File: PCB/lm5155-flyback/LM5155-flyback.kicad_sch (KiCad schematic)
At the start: 31 parts, among them Q1 DMT6030LFCL-7, T1 EP7-5801_750315825, U1 LM5155

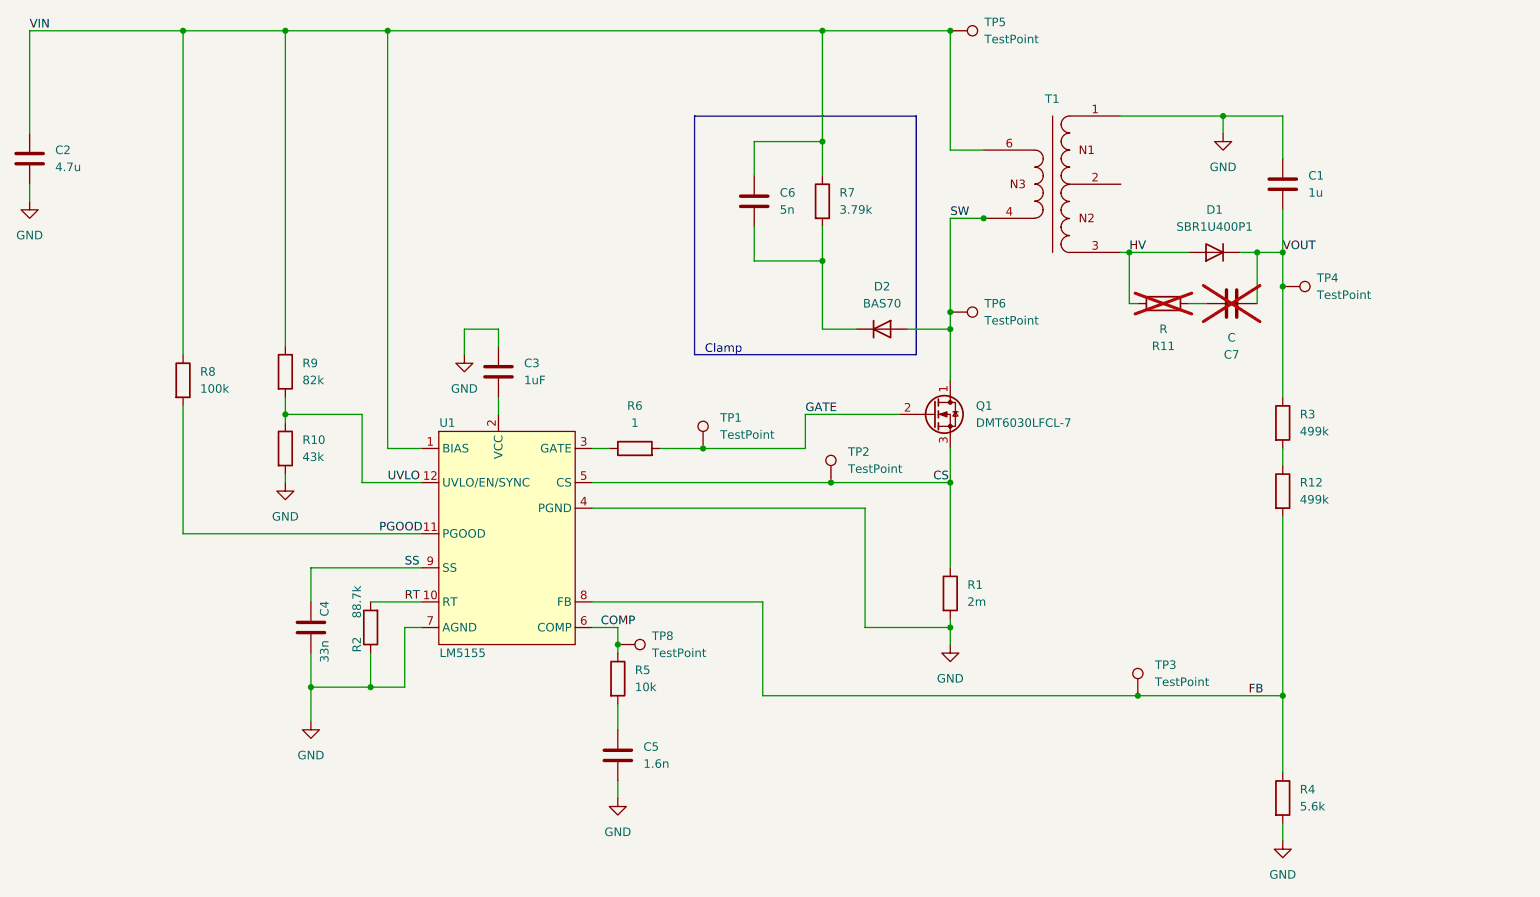
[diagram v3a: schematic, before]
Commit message: Replaced LM5155 with LM5156H. Also replaced MOSFET. Packages just too difficult to solder.
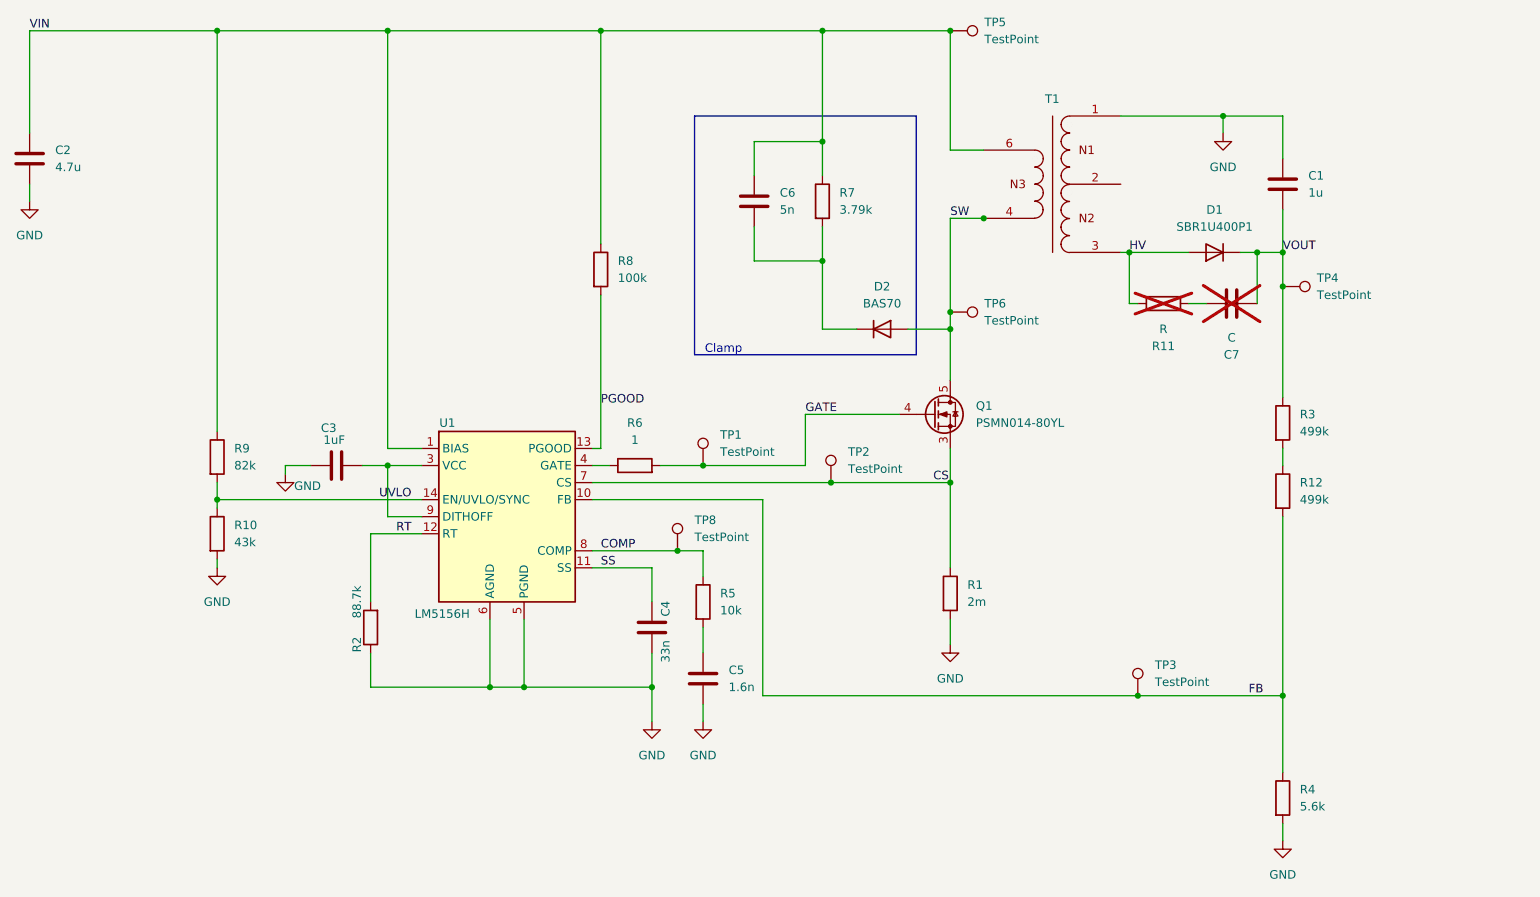
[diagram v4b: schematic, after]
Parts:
- removed Q1: DMT6030LFCL-7, LM5155-flyback:U-DFN1616-6, symbol Transistor_FET:Q_NMOS_DGS
- added Q1: PSMN014-80YL, Package_TO_SOT_SMD:LFPAK56, symbol LM5155-flyback:PSMN014-80YL
- U1: value LM5155 -> LM5156H; footprint LM5155-flyback:WSON-12-1EP_3x2mm_P0.5mm_EP1x2.65_ThermalVias -> Package_SO:Texas_HTSSOP-14-1EP_4.4x5mm_P0.65mm_EP3.4x5mm_Mask3.155x3.255mm_ThermalVias; symbol LM5155-flyback:LM5155 -> Regulator_Switching:LM5156HPWP
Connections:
- net COMP: now also U1.8 (COMP); no longer U1.6 (COMP)
- net CS: now also U1.7 (CS), Q1.1 (S), Q1.2 (S), Q1.3 (S); no longer U1.5 (CS)
- net FB: now also U1.10 (FB); no longer U1.8 (FB)
- net GATE: now also Q1.4 (G)
- net GND: now also U1.15 (AGND), U1.5 (PGND), U1.6 (AGND); no longer U1.13, U1.4 (PGND), U1.7 (AGND)
- net PGOOD: now also U1.13 (PGOOD); no longer U1.11 (PGOOD)
- net RT: now also U1.12 (RT); no longer U1.10 (RT)
- net SS: now also U1.11 (SS); no longer U1.9 (SS)
- net SW: now also Q1.5 (D)
- net UVLO: now also U1.14 (EN/UVLO/SYNC); no longer U1.12 (UVLO/EN/SYNC)
- net at U1.2 (NC): no longer C3.2
- net at U1.3 (VCC): now also C3.2, U1.9 (DITHOFF); no longer R6.1
- new net: R6.1, U1.4 (GATE)
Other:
- moved on the sheet: C3, C4, C5, R10, R5, R6, R8, R9, TP1, TP8

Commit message: updates
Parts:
- added R13, R14: 1Meg, Resistor_SMD:R_0805_2012Metric_Pad1.20x1.40mm_HandSolder, symbol Device:R
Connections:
- net GND: now also R14.2
- net VOUT: now also R13.1
- new net: R13.2, R14.1
